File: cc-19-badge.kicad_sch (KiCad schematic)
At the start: 4 parts, among them IC1 M24SR16-YDW6T_2, J1 Conn_01x06

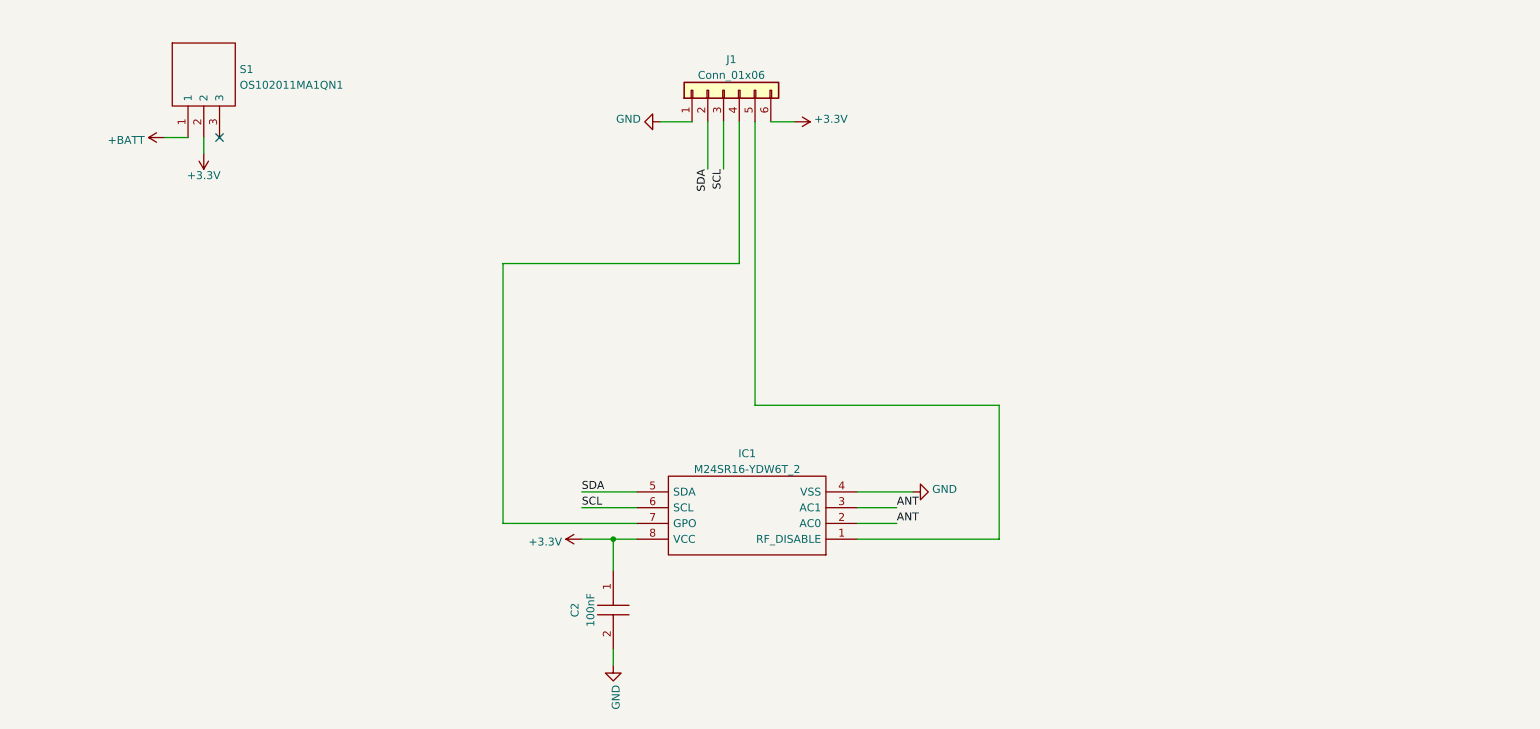
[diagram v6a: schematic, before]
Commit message: Remove debug header (#54)
Co-authored-by: github-actions <github-actions@github.com>
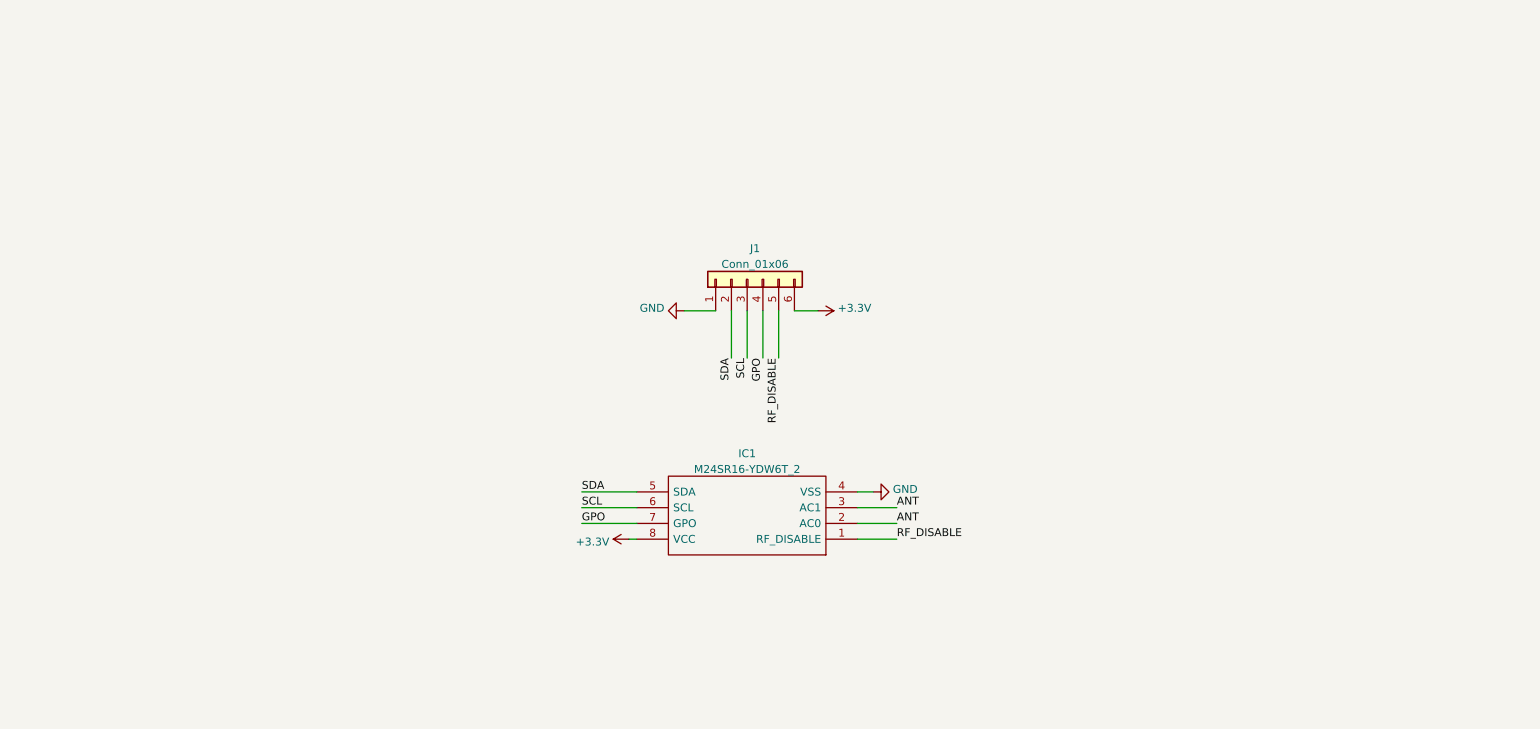
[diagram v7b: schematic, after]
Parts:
- removed C2: 100nF, third-party-schematics:K104K15X7RF5TH5, symbol K104K15X7RF5TH5:K104K15X7RF5TH5
- removed S1: OS102011MA1QN1, third-party-schematics:OS102011MA1QN1, symbol OS102011MA1QN1:OS102011MA1QN1
- IC1: footprint SOP65P640X120-8N -> third-party-schematics:SOP65P640X120-8N
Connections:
- net GPO: now reaches IC1.7 (GPO), J1.4 (Pin_4)
- net RF_DISABLE: now reaches IC1.1 (RF_DISABLE), J1.5 (Pin_5)
- no-connect marks 1 -> 0
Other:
- moved on the sheet: J1
